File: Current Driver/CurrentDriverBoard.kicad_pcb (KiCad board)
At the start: 2 copper layers, 33.5 x 36 mm, 7 parts, among them J1 Laser Diode, J2 POT, J3 Conn_01x02_Pin, U1 LF356

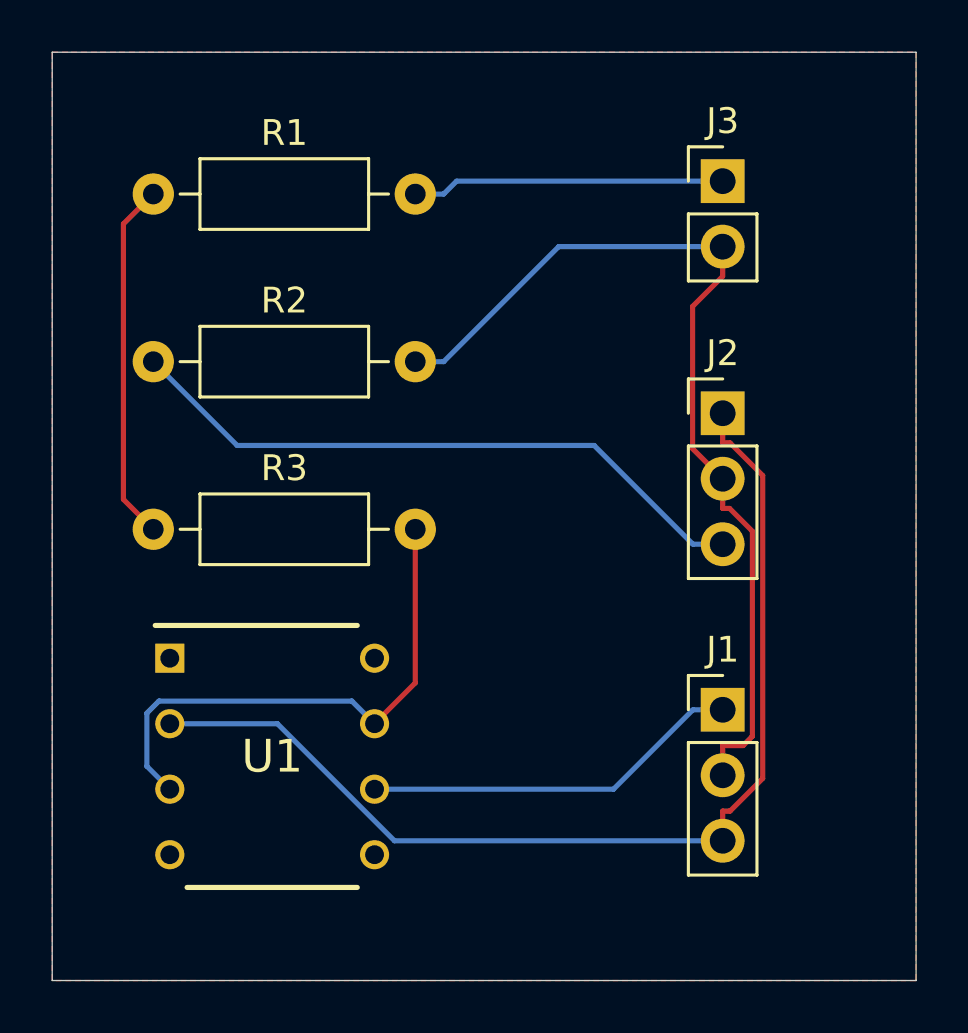
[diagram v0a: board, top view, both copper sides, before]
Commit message: Updating Associated Files. Some files can only be opened in Linux. Sorry Windows Users :P
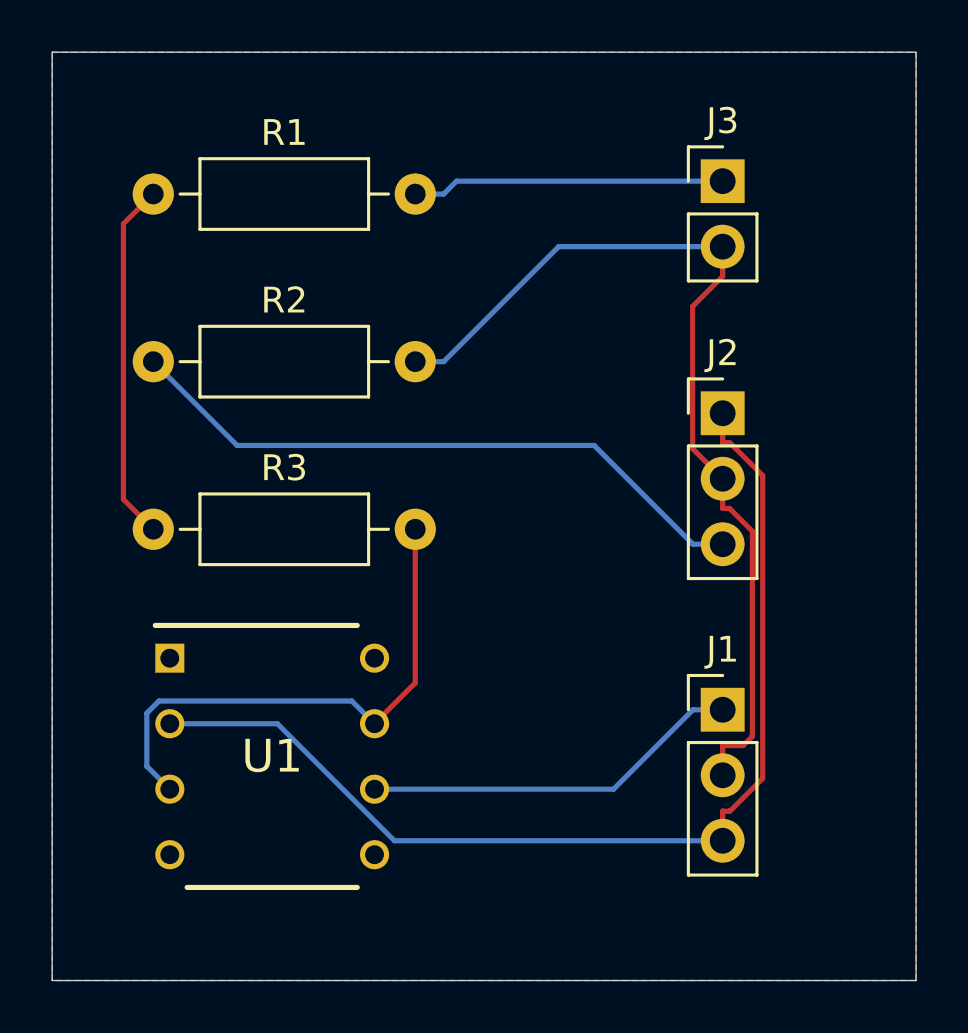
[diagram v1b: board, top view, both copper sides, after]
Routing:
- added copper zone on B.Cu, net Earth
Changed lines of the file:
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@@
 			(outputformat 1)
 			(mirror no)
-			(drillshape 1)
+			(drillshape 0)
 			(scaleselection 1)
-			(outputdirectory "")
+			(outputdirectory "Gerbers and Drills/")
 		)
 	)
@@
 		(connect_pads
 			(clearance 0.5)
+		)
+		(min_thickness 0.25)
+		(filled_areas_thickness no)
+		(fill yes
+			(thermal_gap 0.5)
+			(thermal_bridge_width 0.5)
+		)
+		(polygon
+			(pts
+				(xy 134.5 67.5) (xy 168 67.5) (xy 168 103.5) (xy 134.5 103.5)
+			)
+		)
+	)
+	(zone
+		(net 2)
+		(net_name "Earth")
+		(layer "B.Cu")
+		(hatch edge 0.5)
+		(priority 1)
+		(connect_pads
+			(clearance 0.5)
